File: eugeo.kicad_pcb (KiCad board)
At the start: 2 copper layers, 284.9 x 75.4 mm, 128 parts, among them J1 USB-C, J2 AVR_ISP, SW1 RESET, SW2 BOOT, U1 ATMEGA328P-PU, Y1 16MHz

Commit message: Add centre component cover
Lumberjack-style 2 mm acrylic cover over the diode stacks, MCU and USB-C,
held by four M2 10 mm standoffs. Adds mounting holes H9-H12 to the PCB
(rerouted, DRC clean, 49/49 functional checks), cover outline/DXF/gerbers,
a STEP/STL model, and a clearance check against parts and the case.

Co-Authored-By: Claude Opus 5.5 <noreply@anthropic.com>
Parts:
- added H10: M2, eugeo:MountingHole_M2_NPTH, F.Cu at (173.3, 59.4)
- added H11: M2, eugeo:MountingHole_M2_NPTH, F.Cu at (139.4, 121.6)
- added H12: M2, eugeo:MountingHole_M2_NPTH, F.Cu at (165.4, 121.6)
- added H9: M2, eugeo:MountingHole_M2_NPTH, F.Cu at (131.5, 59.4)
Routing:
- net /CC2: track 13.4 -> 32.0 mm, vias 1 -> 0
- net /COL2: track 347.0 -> 362.5 mm
- net /COL0: track 474.3 -> 465.1 mm, vias 1 -> 2
- net +5V: track 114.6 -> 122.3 mm
- net /USB_D-: track 35.4 -> 28.8 mm, vias 0 -> 1
- net /LED1_A: track 13.0 -> 7.26 mm
- net /COL5: track 235.0 -> 230.3 mm
- net /CC1: track 11.8 -> 7.27 mm
- net /RESET: track 57.9 -> 62.1 mm, vias 1 -> 0
- net GND: track 153.1 -> 156.9 mm
- net /COL3: track 303.4 -> 306.3 mm
- net /ROW2: track 43.6 -> 40.8 mm
- net /LED2: track 42.3 -> 39.9 mm, vias 1 -> 0
- net /ROW6: track 49.3 -> 47.4 mm
- net /LED1: track 39.2 -> 40.9 mm
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
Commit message: Switch to RP2040, zigzag diodes and a frozen-stump back
- MCU: ATmega328P + V-USB -> RP2040 + W25Q16 QSPI flash, 12 MHz crystal,
  MCP1700 3.3 V LDO, USBLC6 ESD and 27R series resistors. SMD parts are
  assembled by JLCPCB (BOM/CPL now include them); everything else stays
  through-hole and on show.
- RP2040 block is hand-routed: +3V3 ring inside the pin ring, +1V1 via the
  back, QSPI / crystal / decoupling / row and column escapes. ISP and SWD
  headers dropped (UF2 flashing over USB with BOOT + RESET).
- Diode stacks zigzag like Lumberjack.
- Back side artwork: frozen tree stump with frost ferns and snowflakes,
  some as bare-copper mask openings (scripts/stump_art.py).
- QMK: RP2040 / rp2040 bootloader, new GP pin map, prebuilt UF2 files.
- verify_design.py rewritten for RP2040 (59 checks), preorder checks 23/23.
- Case support pillar moved clear of U4; cover, plates and laser-cut SVGs
  regenerated for the new cover holes.

Co-Authored-By: Claude Opus 5.5 <noreply@anthropic.com>
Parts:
- removed C4, C5: 100n, Capacitor_THT:C_Disc_D4.3mm_W1.9mm_P5.00mm
- removed D49, D50: 3.6V, Diode_THT:D_DO-35_SOD27_P7.62mm_Horizontal
- removed J2: AVR_ISP, Connector_PinHeader_2.54mm:PinHeader_2x03_P2.54mm_Vertical
- removed R1: 1.5k, Resistor_THT:R_Axial_DIN0204_L3.6mm_D1.6mm_P7.62mm_Horizontal
- removed R4: 10k, Resistor_THT:R_Axial_DIN0204_L3.6mm_D1.6mm_P7.62mm_Horizontal
- added C10: 100n, Capacitor_SMD:C_0402_1005Metric, F.Cu at (147.1, 74.4)
- added C11: 100n, Capacitor_SMD:C_0402_1005Metric, F.Cu at (147.1, 78.0)
- added C12: 100n, Capacitor_SMD:C_0402_1005Metric, B.Cu at (151.3, 80.6)
- added C13: 100n, Capacitor_SMD:C_0402_1005Metric, B.Cu at (154.5, 80.6)
- added C14: 100n, Capacitor_SMD:C_0402_1005Metric, F.Cu at (157.7, 78.0)
- added C15: 100n, Capacitor_SMD:C_0402_1005Metric, F.Cu at (157.7, 74.4)
- added C17: 1u, Capacitor_SMD:C_0402_1005Metric, F.Cu at (156.3, 72.7)
- added C18: 1u, Capacitor_SMD:C_0402_1005Metric, F.Cu at (154.4, 70.7)
- added C20: 100n, Capacitor_SMD:C_0402_1005Metric, F.Cu at (152.8, 70.6)
- added C22: 100n, Capacitor_SMD:C_0402_1005Metric, F.Cu at (141.6, 73.2)
- added C6: 1u, Capacitor_THT:C_Disc_D3.0mm_W2.0mm_P2.50mm, F.Cu at (143.4, 95.6)
- added C7: 1u, Capacitor_THT:C_Disc_D3.0mm_W2.0mm_P2.50mm, F.Cu at (143.4, 92.8)
- added R10: 1k, Resistor_THT:R_Axial_DIN0204_L3.6mm_D1.6mm_P7.62mm_Horizontal, F.Cu at (152.6, 103.2)
- added R11: 1k, Resistor_SMD:R_0402_1005Metric, F.Cu at (152.6, 82.5)
- added R9: 10k, Resistor_THT:R_Axial_DIN0204_L3.6mm_D1.6mm_P7.62mm_Horizontal, F.Cu at (150.2, 103.2)
- added U2: W25Q16JVSSIQ, Package_SO:SOIC-8_5.3x5.3mm_P1.27mm, F.Cu at (145.2, 69.6)
- added U3: MCP1700-3302E, Package_TO_SOT_THT:TO-92_Inline_Wide, F.Cu at (145.6, 90.2)
- added U4: USBLC6-2SC6, Package_TO_SOT_SMD:SOT-23-6, B.Cu at (152.4, 65.6)
- C3: value 4.7u -> 10u
- R2, R3: value 75R -> 27R
- R7, R8: value 1.5k -> 1k
- U1: value ATMEGA328P-PU -> RP2040; footprint Package_DIP:DIP-28_W7.62mm -> Package_DFN_QFN:QFN-56-1EP_7x7mm_P0.4mm_EP3.2x3.2mm
- Y1: value 16MHz -> 12MHz
- moved F1 36.6 mm to (155.0, 101.8), turned to 90 degrees
- moved SW1 29.4 mm to (143.0, 105.0)
- moved R2 20.7 mm to (158.6, 57.0)
- moved R8 18.2 mm to (161.8, 96.4), turned to -90 degrees
- moved R7 15.7 mm to (159.6, 96.4), turned to -90 degrees
- moved C2 11.6 mm to (155.0, 92.6), turned to 0 degrees
- moved LED1 9.71 mm to (159.6, 109.5), turned to 90 degrees
- moved C3 9.04 mm to (156.2, 118.0)
- moved SW2 7.92 mm to (143.0, 115.0)
- moved C1 6.11 mm to (150.0, 92.6), turned to 0 degrees
- moved U1 5.91 mm to (152.4, 77.0)
- moved H12 4.25 mm to (162.2, 118.8)
- moved H11 4.25 mm to (142.6, 118.8)
- moved LED2 3.89 mm to (161.8, 114.6), turned to 90 degrees
- moved Y1 3.19 mm to (151.4, 88.0), turned to 0 degrees
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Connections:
- C1 pad 1: /XTAL2 -> /XIN
- C2 pad 1: /XTAL1 -> /XOUT_X
- SW1 pad 1: /RESET -> /RUN
- SW2 pad 1: /ROW3 -> /BOOTSEL
- U1 pad 1: /RESET -> +3V3
- U1 pad 10: /XTAL2 -> +3V3
- U1 pad 11: /ROW3 -> unconnected-(U1-GPIO8-Pad11)
- U1 pad 12: /COL5 -> /COL0
- U1 pad 13: /COL4 -> /COL1
- U1 pad 14: /COL3 -> /COL2
- U1 pad 15: /ROW7 -> unconnected-(U1-GPIO12-Pad15)
- U1 pad 16: /COL2 -> unconnected-(U1-GPIO13-Pad16)
- U1 pad 17: /COL1 -> unconnected-(U1-GPIO14-Pad17)
- U1 pad 18: /COL0 -> unconnected-(U1-GPIO15-Pad18)
- U1 pad 19: /ROW6 -> GND
- U1 pad 2: /ROW0 -> unconnected-(U1-GPIO0-Pad2)
- U1 pad 20: +5V -> /XIN
- U1 pad 21: unconnected-(U1-AREF-Pad21) -> /XOUT
- U1 pad 22: GND -> +3V3
- U1 pad 23: unconnected-(U1-PC0-Pad23) -> /+1V1
- U1 pad 24: /ROW5 -> unconnected-(U1-SWCLK-Pad24)
- U1 pad 26: /LED2 -> /RUN
- U1 pad 28: /ROW4 -> /LED2
- U1 pad 3: /ROW1 -> /ROW0
- U1 pad 4: /USB_D+ -> unconnected-(U1-GPIO2-Pad4)
- U1 pad 5: /USB_D- -> /ROW1
- U1 pad 6: /ROW2 -> unconnected-(U1-GPIO4-Pad6)
- U1 pad 7: +5V -> /ROW2
- U1 pad 8: GND -> /ROW3
- U1 pad 9: /XTAL1 -> unconnected-(U1-GPIO7-Pad9)
- Y1 pad 1: /XTAL1 -> /XIN
- Y1 pad 2: /XTAL2 -> /XOUT_X
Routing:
- net GND: track 156.9 -> 29.3 mm, vias 0 -> 12
- net +3V3: track 0.00 -> 76.1 mm, vias 0 -> 3
- net +5V: track 122.3 -> 47.8 mm, vias 0 -> 1
- net /RESET: track 62.1 -> 0.00 mm
- net /RUN: track 0.00 -> 43.8 mm, vias 0 -> 1
- net /QSPI_SS: track 0.00 -> 41.1 mm, vias 0 -> 2
- net /VBUS: track 14.5 -> 52.7 mm, vias 2 -> 3
- net /ROW7: track 26.3 -> 63.2 mm
- net /COL3: track 306.3 -> 334.3 mm, vias 1 -> 3
- net /COL4: track 265.7 -> 292.3 mm, vias 2 -> 3
- net /QSPI_SD3: track 0.00 -> 25.2 mm
- net /BOOTSEL: track 0.00 -> 25.1 mm
- net /CC2: track 32.0 -> 9.68 mm, vias 0 -> 1
- net /QSPI_SCLK: track 0.00 -> 21.9 mm
- net /COL5: track 230.3 -> 250.3 mm, vias 0 -> 3
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- added copper zone on F.Cu, net GND
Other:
- board text removed: "GND MOSI VCC"
- board text removed: "RST SCK MISO"

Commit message: Move the status LEDs to the top, side by side
LED1 / LED2 now sit next to each other above the QSPI flash. They are
driven from the two topmost left GPIOs (GP2 / GP1) through 0402 resistors
on the back, which frees the crowded bottom-right corner. Left rows move
to GP3-GP6; QMK pins and the UF2 builds follow.

Co-Authored-By: Claude Opus 5.5 <noreply@anthropic.com>
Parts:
- R7, R8: footprint Resistor_THT:R_Axial_DIN0204_L3.6mm_D1.6mm_P7.62mm_Horizontal -> Resistor_SMD:R_0402_1005Metric; moved to B.Cu
- moved LED2 55.1 mm to (143.6, 62.6), turned to 0 degrees
- moved LED1 51.4 mm to (138.6, 62.6), turned to 0 degrees
- moved R8 33.0 mm to (145.4, 67.8), turned to 90 degrees
- moved R7 30.4 mm to (144.6, 70.0), turned to 90 degrees
- moved R6 0.60 mm to (138.6, 58.9)
- moved R5 0.40 mm to (138.6, 56.6)
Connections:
- U1 pad 27: /LED1 -> unconnected-(U1-GPIO16-Pad27)
- U1 pad 28: /LED2 -> unconnected-(U1-GPIO17-Pad28)
- U1 pad 3: /ROW0 -> /LED2
- U1 pad 4: unconnected-(U1-GPIO2-Pad4) -> /LED1
- U1 pad 5: /ROW1 -> /ROW0
- U1 pad 6: unconnected-(U1-GPIO4-Pad6) -> /ROW1
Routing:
- net /COL5: track 250.3 -> 266.8 mm
- net /LED2: track 22.8 -> 10.1 mm, vias 0 -> 1
- net /LED1: track 21.0 -> 8.87 mm, vias 0 -> 1
- net /QSPI_SS: track 41.1 -> 50.9 mm
- net /LED1_A: track 2.94 -> 10.4 mm
- net /CONN_D-: track 24.7 -> 19.4 mm, vias 1 -> 0
- net /CONN_D+: track 18.0 -> 23.2 mm, vias 1 -> 2
- net +3V3: track 76.1 -> 72.2 mm, vias 3 -> 4
- net /LED2_A: track 8.04 -> 5.00 mm
- net +5V: track 47.8 -> 45.9 mm, vias 1 -> 0
- net /BOOTSEL: track 25.1 -> 23.4 mm
- net /VBUS: track 52.7 -> 54.3 mm, vias 3 -> 2

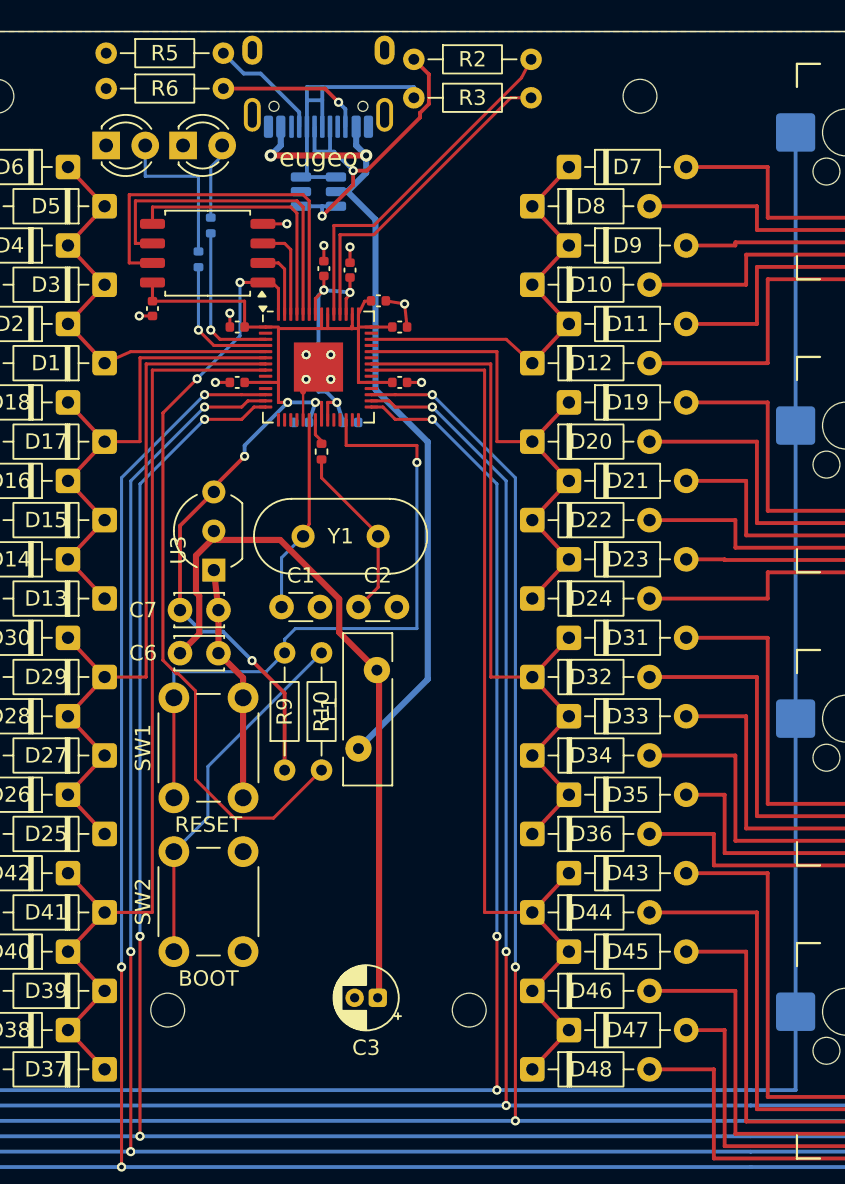
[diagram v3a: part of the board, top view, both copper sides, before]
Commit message: Balance the centre layout: LEDs left and right, parts mirrored
- One LED on each side at the top (under R5/R6 and R2/R3), driven from the
  topmost left / right GPIO (GP1 / GP28); right rows move to GP23-GP26.
- USB D+/D- go round the right LED to R2/R3.
- Lower parts mirrored about the centre line: U3 | crystal | F1, the four
  disc capacitors in one row, R9 / R10 between RESET and BOOT, C3 centred.

Co-Authored-By: Claude Opus 5.5 <noreply@anthropic.com>
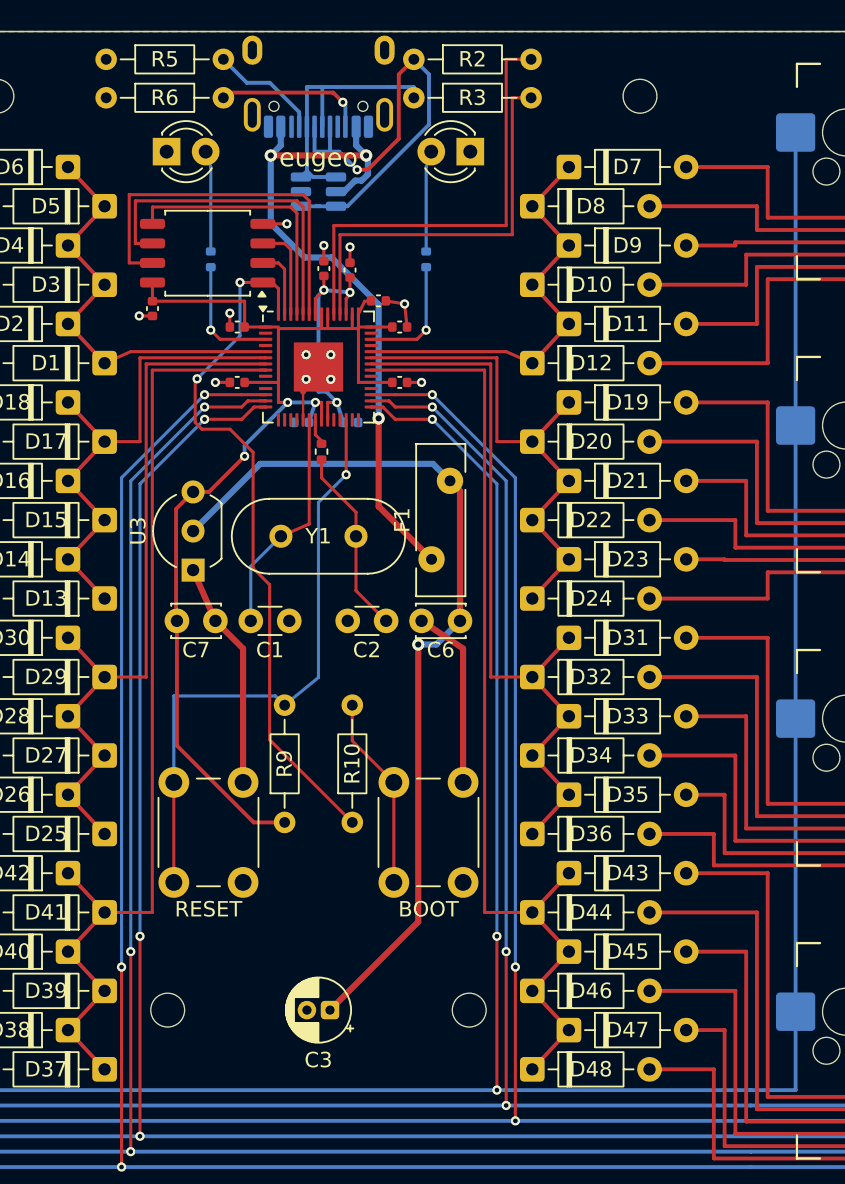
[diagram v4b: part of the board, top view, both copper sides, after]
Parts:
- moved LED2 18.7 mm to (162.3, 63.0), turned to 180 degrees
- moved C6 18.3 mm to (161.6, 93.5), turned to 180 degrees
- moved SW2 15.0 mm to (157.3, 110.5)
- moved R8 14.2 mm to (159.4, 70.0)
- moved F1 13.2 mm to (159.8, 89.5)
- moved SW1 5.50 mm to (143.0, 110.5)
- moved LED1 3.95 mm to (142.5, 63.0)
- moved R10 3.94 mm to (154.6, 106.6)
- moved R9 3.40 mm to (150.2, 106.6)
- moved C3 3.20 mm to (153.2, 118.8)
- moved C1 2.19 mm to (148.0, 93.5)
- moved C2 2.01 mm to (156.8, 93.5), turned to 180 degrees
- moved Y1 1.44 mm to (150.0, 88.0)
- moved U3 1.35 mm to (144.2, 90.2)
- moved R7 0.80 mm to (145.4, 70.0)
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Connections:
- U1 pad 3: /LED2 -> /LED1
- U1 pad 37: unconnected-(U1-GPIO25-Pad37) -> /ROW5
- U1 pad 38: /ROW5 -> /ROW4
- U1 pad 4: /LED1 -> unconnected-(U1-GPIO2-Pad4)
- U1 pad 40: /ROW4 -> /LED2
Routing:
- net /COL5: track 266.8 -> 250.3 mm
- net +5V: track 45.9 -> 57.8 mm, vias 0 -> 1
- net GND: track 29.3 -> 40.6 mm
- net /BOOTSEL: track 23.4 -> 12.6 mm
- net /VBUS: track 54.3 -> 46.3 mm, vias 2 -> 3
- net /CONN_D+: track 23.2 -> 30.8 mm, vias 2 -> 1
- net /USB_D+: track 23.3 -> 29.4 mm
- net /USB_D-: track 21.3 -> 26.5 mm
- net +3V3: track 72.2 -> 76.6 mm, vias 4 -> 3
- net /QSPI_SS: track 50.9 -> 46.7 mm
- net /RUN: track 43.8 -> 39.9 mm
- net /LED1_A: track 10.4 -> 6.54 mm
- net /XIN: track 12.8 -> 15.1 mm
- net /LED2: track 10.1 -> 7.90 mm
- net /LED2_A: track 5.00 -> 6.54 mm
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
